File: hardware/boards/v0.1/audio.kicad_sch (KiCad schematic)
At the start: 29 parts, among them J4 SPKR_L, J5 SPKR_R, J8 LINE_OUT, J9 LINE_IN, U24 MIC, U28 TS5A23159RSE, U29 NAU88C22YG

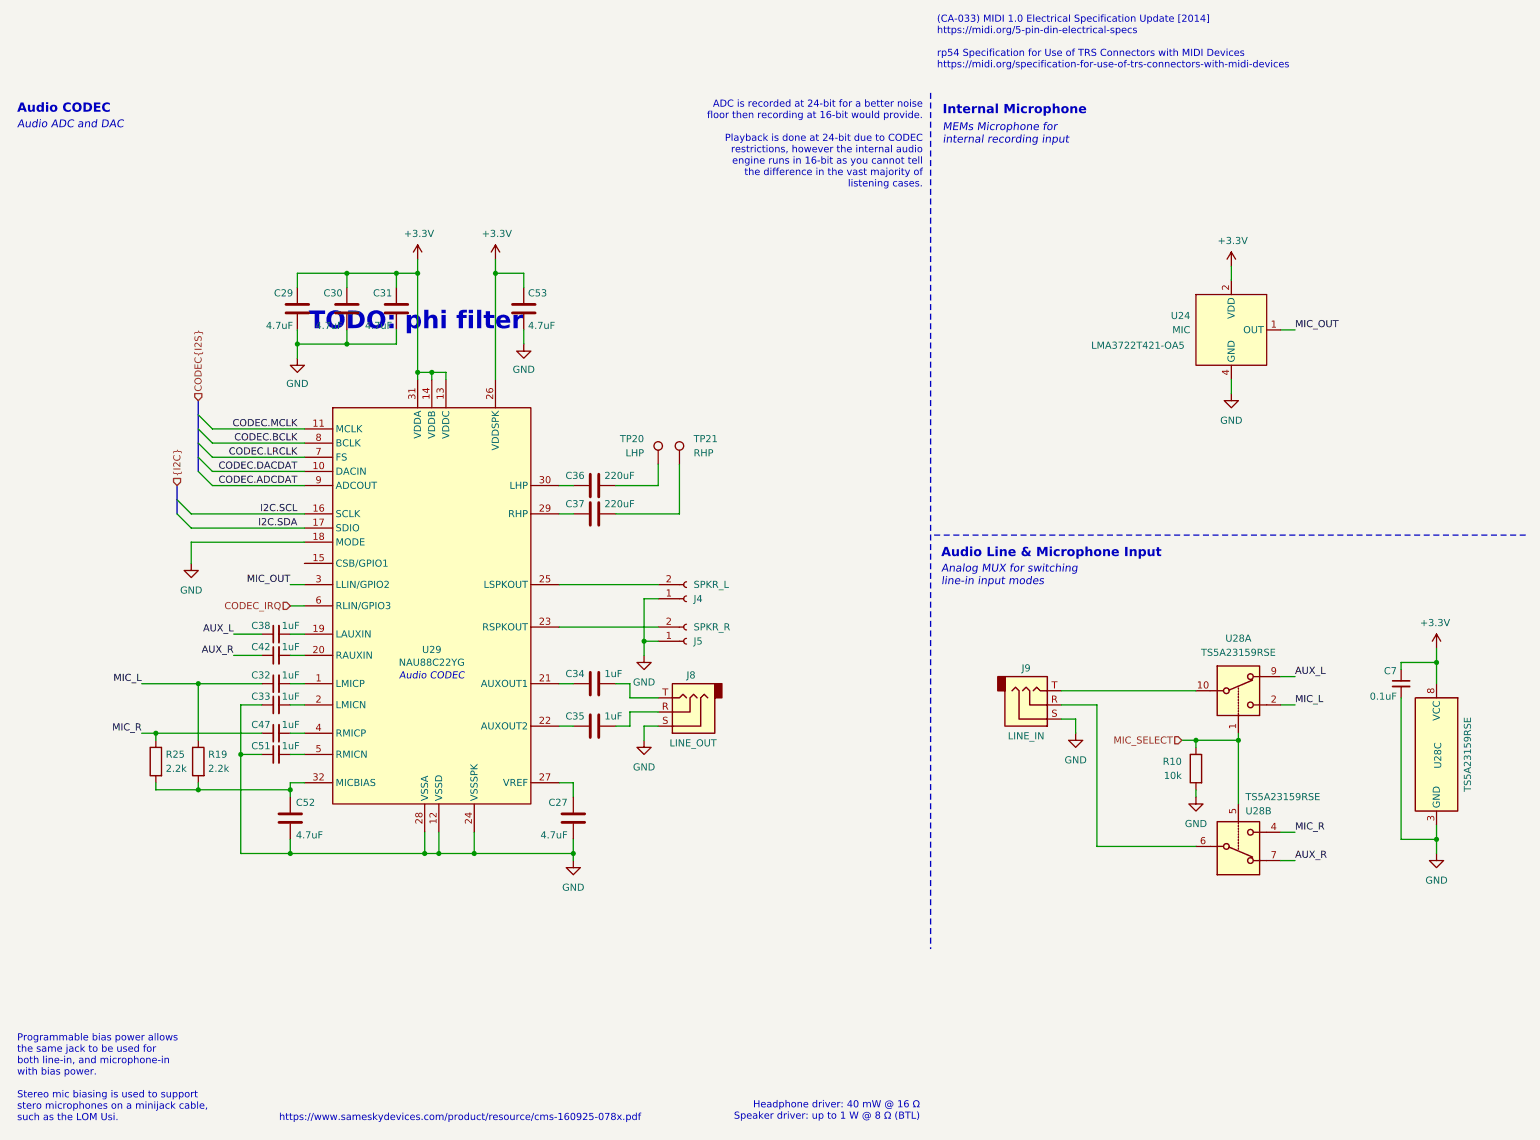
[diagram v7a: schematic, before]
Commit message: feat: FM receiver routing
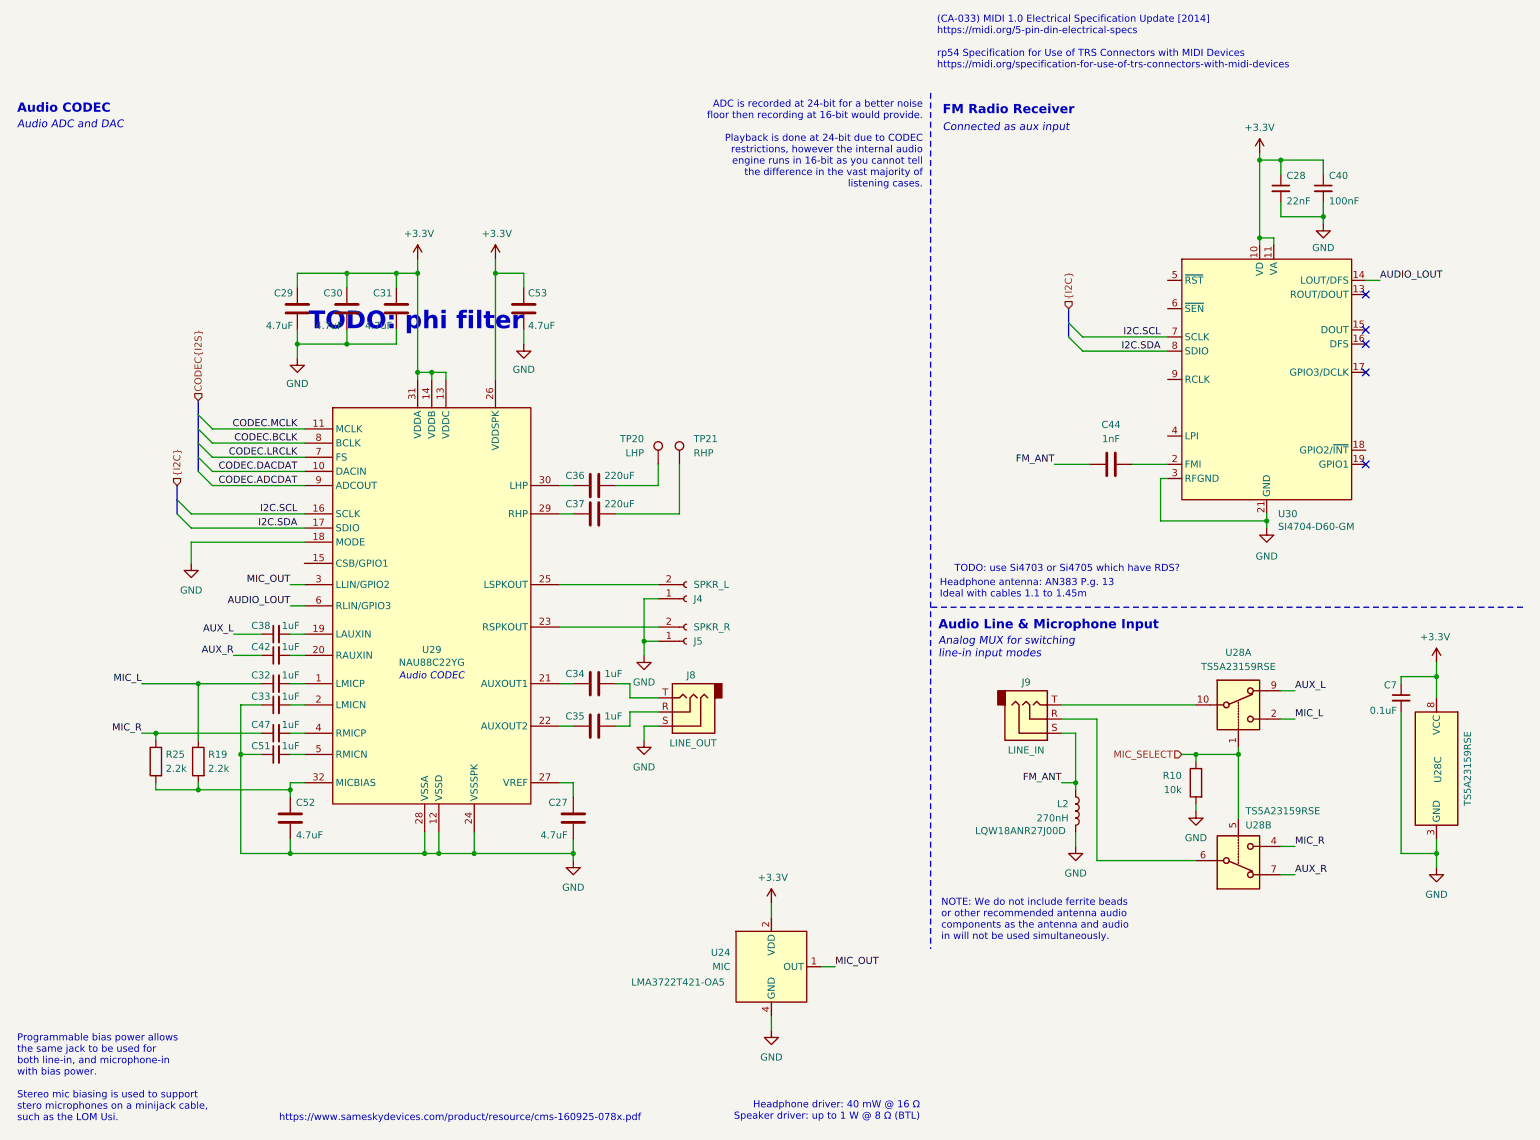
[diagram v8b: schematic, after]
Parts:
- added C28: 22nF, Capacitor_SMD:C_0603_1608Metric, symbol Device:C_Small
- added C40: 100nF, Capacitor_SMD:C_0603_1608Metric, symbol Device:C_Small
- added C44: 1nF, Capacitor_SMD:C_0603_1608Metric, symbol Device:C
- added L2: 270nH, Inductor_SMD:L_0603_1608Metric, symbol Device:L
- added U30: SI4704-D60-GM, pocket_synth:SI4704-D60-GMR, symbol pocket_synth:SI4704-D60-GM
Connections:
- net +3.3V: now also C28.1, C40.1, U30.10 (VD), U30.11 (VA)
- net GND: now also C28.2, C40.2, L2.2, U30.12 (GND), U30.21 (GND), U30.3 (RFGND); no longer J9.S
- net I2C.SCL: now also U30.7 (SCLK)
- net I2C.SDA: now also U30.8 (SDIO)
- net CODEC_IRQ renamed AUDIO_LOUT
- net AUDIO_LOUT: now also U30.14 (LOUT/DFS)
- new net: C44.2, U30.2 (FMI)
- new net FM_ANT: C44.1, J9.S, L2.1
- no-connect marks 0 -> 5
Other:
- note added: "Connected as aux input"
- note added: "FM Radio Receiver"
- note added: "Headphone antenna: AN383 P.g. 13 Ideal with cables 1.1 to 1.45m"
- note added: "NOTE: We do not include ferrite beads or other recommended antenna audio components as the antenna and audio in will not be used simultaneously."
- note added: "TODO: use Si4703 or Si4705 which have RDS?"
- note removed: "Internal Microphone"
- note removed: "MEMs Microphone for internal recording input"
- moved on the sheet: C7, J9, R10, U24, U28A, U28B, U28C
